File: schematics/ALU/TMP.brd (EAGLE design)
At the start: 73.3 x 44.7 mm, 11 parts

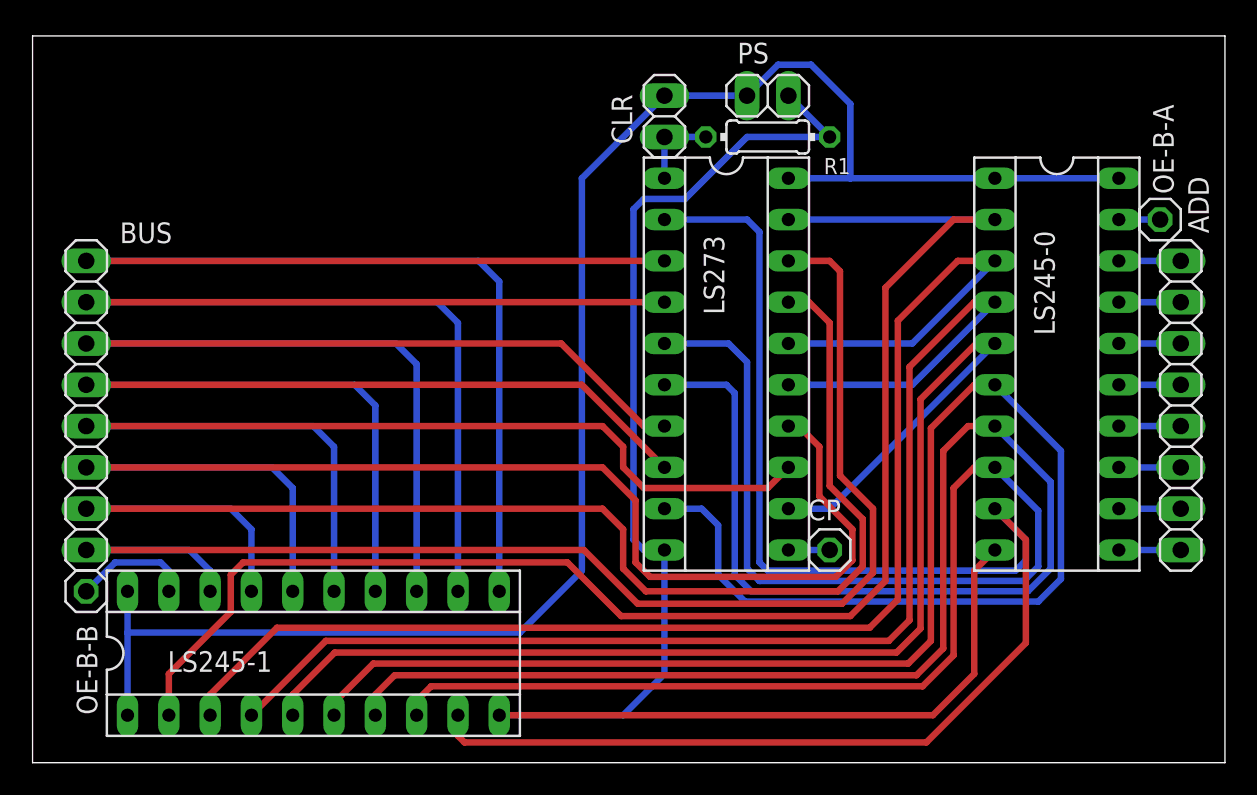
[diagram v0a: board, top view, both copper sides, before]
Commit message: TMP (B) register doesnt need buffers.
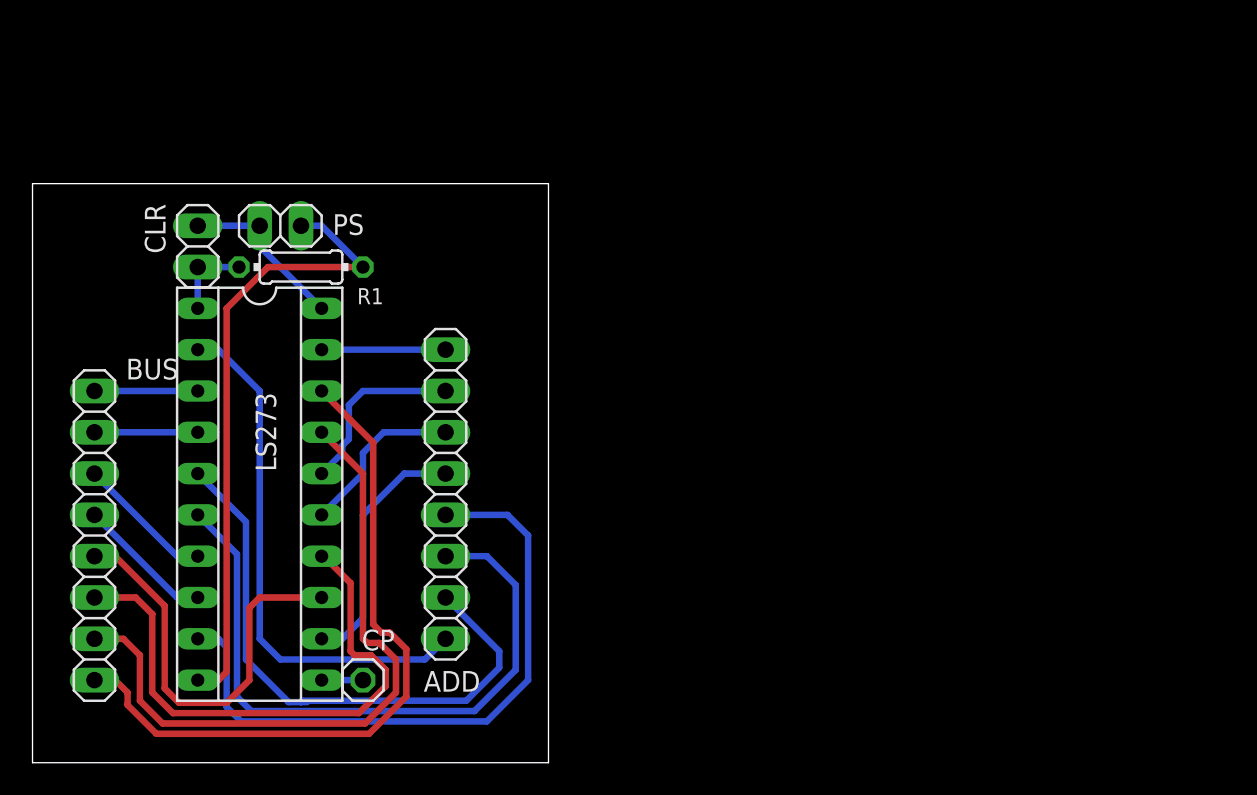
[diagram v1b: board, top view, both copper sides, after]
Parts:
- removed LS245-0, LS245-1: (no value), ic-package:SOCKET-20
- removed OE-B-A, OE-B-B: (no value), pinhead:1X01
- moved ADD 45.5 mm to (25.4, 16.5)
- moved PS 31.0 mm to (15.2, 33.0)
- moved CLR 29.8 mm to (10.2, 31.8)
- moved R1 29.8 mm to (16.5, 30.5)
- moved CP 29.8 mm to (20.3, 5.08)
- moved LS273 29.8 mm to (14.0, 16.5)
- moved BUS 8.02 mm to (3.81, 14.0)
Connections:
- removed net A0: ADD.1, LS245-0.18
- removed net A1: ADD.2, LS245-0.17
- removed net A2: ADD.3, LS245-0.16
- removed net A3: ADD.4, LS245-0.15
- removed net A4: ADD.5, LS245-0.14
- removed net A5: ADD.6, LS245-0.13
- removed net A6: ADD.7, LS245-0.12
- removed net A7: ADD.8, LS245-0.11
- removed net B-A: LS245-0.19, OE-B-A.1
- removed net B-B: LS245-1.19, OE-B-B.1
- net B0: no longer LS245-1.11
- net B1: no longer LS245-1.12
- net B2: no longer LS245-1.13
- net B3: no longer LS245-1.14
- net B4: no longer LS245-1.15
- net B5: no longer LS245-1.16
- net B6: no longer LS245-1.17
- net B7: no longer LS245-1.18
- net GND: no longer LS245-0.10, LS245-1.10
- net Q0: now also ADD.8; no longer LS245-0.9, LS245-1.9
- net Q1: now also ADD.7; no longer LS245-0.8, LS245-1.8
- net Q2: now also ADD.6; no longer LS245-0.7, LS245-1.7
- net Q3: now also ADD.5; no longer LS245-0.6, LS245-1.6
- net Q4: now also ADD.4; no longer LS245-0.5, LS245-1.5
- net Q5: now also ADD.3; no longer LS245-0.4, LS245-1.4
- net Q6: now also ADD.2; no longer LS245-0.3, LS245-1.3
- net Q7: now also ADD.1; no longer LS245-0.2, LS245-1.2
- net VCC: no longer LS245-0.1, LS245-0.20, LS245-1.1, LS245-1.20
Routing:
- net VCC: track 106.6 -> 10.5 mm
- net Q7: track 92.3 -> 7.62 mm
- net Q6: track 85.4 -> 11.2 mm
- net B0: track 80.5 -> 6.35 mm
- net Q5: track 80.2 -> 10.5 mm
- net B1: track 75.5 -> 6.35 mm
- net B2: track 72.5 -> 8.45 mm
- net Q4: track 78.6 -> 15.5 mm
- net Q0: track 95.2 -> 32.6 mm
- net Q3: track 99.9 -> 40.1 mm
- net B3: track 67.4 -> 8.45 mm
- net Q2: track 99.6 -> 41.0 mm
- net GND: track 97.2 -> 38.6 mm
- net Q1: track 92.5 -> 36.3 mm
- net B5: track 82.4 -> 34.7 mm
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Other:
- board size 73.3 x 44.7 mm -> 31.7 x 35.6 mm
